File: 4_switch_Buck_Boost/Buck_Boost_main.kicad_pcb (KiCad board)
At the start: 2 copper layers, 12 parts, among them J1 Screw_Terminal_2x5.08, J2 Screw_Terminal_2x5.08, J3 Screw_Terminal_2x2.54, Q1 CSD18532Q5B, Q2 CSD18532Q5B, Q3 CSD18532Q5B, Q4 CSD18532Q5B, U1 LT8390EUFD_PBF

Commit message: Updated Schematic with cool stuff trust
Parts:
- removed F1, F2: Fuse_Holder_Auto, rsx_fuses:FUSE_3568-10
- removed HW1: Board_Mount_Heat_Sink_Screw_2.5C/W, rsx_misc:ATS-1139-C1-R0
- removed J1, J2: Screw_Terminal_2x5.08, rsx_headers_screw:Molex_0398800302
- removed J3: Screw_Terminal_2x2.54, rsx_headers_screw:Wurth_691210910002
- removed L1: 15u, rsx_inductors:PQ2617BHA-XXXK
- removed Q1, Q2, Q3, Q4: CSD18532Q5B, Package_TO_SOT_SMD:TDSON-8-1
- removed U1: LT8390EUFD_PBF, LT:QFN50P500X400X80-29N
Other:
- copper layers 2 -> 4
- board text removed: "Test1234"

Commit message: Updated the Component Placement
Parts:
- added C1: 4.7u, rsx_capacitors:C_0805_2012Metric, F.Cu at (71.5, 21.7)
- added C101: 4.7u, rsx_capacitors:C_0805_2012Metric, F.Cu at (71.5, 30.8)
- added C102: 0.1u, rsx_capacitors:C_0603_1608Metric, F.Cu at (32.7, 67.5)
- added C103: 0.47u, rsx_capacitors:C_0603_1608Metric, F.Cu at (32.7, 70.0)
- added C106: 4.7u, rsx_capacitors:C_0805_2012Metric, F.Cu at (71.5, 33.8)
- added C107: 47u, Capacitor_SMD:CP_Elec_8x10.5, F.Cu at (24.1, 25.2)
- added C108: 47u, Capacitor_SMD:CP_Elec_8x10.5, F.Cu at (24.1, 35.3)
- added C109: 33u, Capacitor_SMD:CP_Elec_8x10.5, F.Cu at (24.1, 45.4)
- added C110: 33u, Capacitor_SMD:CP_Elec_8x10.5, F.Cu at (24.1, 55.4)
- added C111: 33u, Capacitor_SMD:CP_Elec_8x10.5, F.Cu at (24.1, 65.5)
- added C112: 4.7u, rsx_capacitors:C_0805_2012Metric, F.Cu at (52.5, 140.4)
- added C113: 4.7u, rsx_capacitors:C_0805_2012Metric, F.Cu at (55.0, 140.4)
- added C114: 0.1u, rsx_capacitors:C_0603_1608Metric, F.Cu at (32.7, 72.5)
- added C115: 0.1u, rsx_capacitors:C_0603_1608Metric, F.Cu at (32.7, 75.0)
- added C116: 0.1u, rsx_capacitors:C_0603_1608Metric, F.Cu at (36.7, 57.4)
- added C117: 47u, Capacitor_SMD:CP_Elec_8x10.5, F.Cu at (24.1, 75.5)
- added C118: 0.1u, rsx_capacitors:C_0603_1608Metric, F.Cu at (57.0, 140.2)
- added C119: 100p, rsx_capacitors:C_0603_1608Metric, F.Cu at (36.7, 62.5)
- added C120: 4.7n, rsx_capacitors:C_0603_1608Metric, F.Cu at (36.7, 65.0)
- added C121: 0.1u, rsx_capacitors:C_0603_1608Metric, F.Cu at (36.7, 67.5)
- added C123: 470p, Capacitor_SMD:C_0805_2012Metric, F.Cu at (55.0, 133.0)
- added C124: 470p, Capacitor_SMD:C_0805_2012Metric, F.Cu at (97.5, 123.5)
- added C129: 0.1u, rsx_capacitors:C_0603_1608Metric, F.Cu at (36.7, 70.0)
- added C131: 22n, rsx_capacitors:C_0603_1608Metric, F.Cu at (36.7, 72.5)
- added C132: 0.1u, rsx_capacitors:C_0603_1608Metric, F.Cu at (59.0, 140.2)
- added C4: 22n, rsx_capacitors:C_0603_1608Metric, F.Cu at (61.0, 140.2)
- added C5: 0.1u, rsx_capacitors:C_0603_1608Metric, F.Cu at (32.7, 60.0)
- added C6: 1.0u, rsx_capacitors:C_0805_2012Metric, F.Cu at (71.5, 24.7)
- added C7: 1.0u, rsx_capacitors:C_0805_2012Metric, F.Cu at (71.5, 27.8)
- added C8: 0.47u, rsx_capacitors:C_0603_1608Metric, F.Cu at (32.7, 62.5)
- added C9: 0.47u, rsx_capacitors:C_0603_1608Metric, F.Cu at (32.7, 65.0)
- added D1: LED_G, rsx_leds:LED_0805_2012Metric, F.Cu at (24.3, 82.0)
- added D2: LED_G, rsx_leds:LED_0805_2012Metric, F.Cu at (24.3, 85.1)
- added D3: LED_G, rsx_leds:LED_0805_2012Metric, F.Cu at (24.3, 88.1)
- added F1: Fuse_Holder_Auto, Fuse:Fuseholder_Blade_Mini_Keystone_3568, F.Cu at (70.8, 58.6)
- added F2: Fuse_Holder_Auto, Fuse:Fuseholder_Blade_Mini_Keystone_3568, F.Cu at (70.8, 66.9)
- added F3: 40mm_by_20mm_Fan_Vertical, rsx_misc:40mmFan, F.Cu at (51.2, 51.7)
- added H1: M4 PLATED, MountingHole:MountingHole_3.2mm_M3_Pad_Via, F.Cu at (54.8, 60.2)
- added H2: M4 PLATED, MountingHole:MountingHole_3.2mm_M3_Pad_Via, F.Cu at (54.8, 68.1)
- added H3: M4 PLATED, MountingHole:MountingHole_3.2mm_M3_Pad_Via, F.Cu at (54.8, 76.1)
- added H4: M4 PLATED, MountingHole:MountingHole_3.2mm_M3_Pad_Via, F.Cu at (54.8, 84.0)
- added HW2: Board_Mount_Heat_Sink_Adhesive, rsx_misc:BDN10-3CB_A01, F.Cu at (31.5, 46.4)
- added J1: Conn_02x02_Counter_Clockwise, Connector_PinHeader_1.00mm:PinHeader_2x02_P1.00mm_Vertical, F.Cu at (66.2, 39.9)
- added J2: Screw_Terminal_2x5.08, rsx_headers_screw:Molex_0398800302, F.Cu at (60.9, 24.8)
- added J3: Screw_Terminal_2x2.54, rsx_headers_screw:Wurth_691210910002, F.Cu at (60.6, 42.3)
- added J4: Screw_Terminal_2x5.08, rsx_headers_screw:Molex_0398800302, F.Cu at (60.9, 33.8)
- added L1: 15u, Inductor_SMD:L_Wuerth_WE-XHMI-8080, F.Cu at (72.5, 128.5)
- added M1: Fan, Connector_Molex:Molex_KK-396_5273-02A_1x02_P3.96mm_Vertical, F.Cu at (69.6, 79.4)
- added NT1: NetTie_2, rsx_misc:NetTie-2_SMD_Pad0.5mm, F.Cu at (66.1, 43.4)
- added Q1: CSD18532Q5B, Package_TO_SOT_SMD:TDSON-8-1, F.Cu at (64.9, 138.1)
- added Q101: 2N7002K, rsx_packages_TO_SOT:SOT-23, F.Cu at (61.2, 85.2)
- added Q103: BSS83P, Package_TO_SOT_SMD:SOT-23, F.Cu at (80.6, 27.2)
- added Q2: CSD18532Q5B, Package_TO_SOT_SMD:TDSON-8-1, F.Cu at (103.8, 129.0)
- added Q3: CSD18532Q5B, Package_TO_SOT_SMD:TDSON-8-1, F.Cu at (59.0, 135.0)
- added Q4: CSD18532Q5B, Package_TO_SOT_SMD:TDSON-8-1, F.Cu at (94.8, 129.0)
- added Q6: AO3400A, Package_TO_SOT_SMD:SOT-23, F.Cu at (80.6, 22.6)
- added R1: 4.7k, rsx_resistors:R_0603_1608Metric, F.Cu at (40.8, 57.4)
- added R10: 50k, rsx_resistors:R_0603_1608Metric, F.Cu at (40.8, 75.0)
- added R103: 200k, rsx_resistors:R_0603_1608Metric, F.Cu at (44.8, 57.4)
- added R104: 10k, rsx_resistors:R_0603_1608Metric, F.Cu at (44.8, 60.0)
- added R105: 100K, rsx_resistors:R_0603_1608Metric, F.Cu at (44.8, 62.5)
- added R106: 100K, rsx_resistors:R_0603_1608Metric, F.Cu at (44.8, 65.0)
- added R107: 100K, rsx_resistors:R_0603_1608Metric, F.Cu at (44.8, 67.5)
- added R109: 100K, rsx_resistors:R_0603_1608Metric, F.Cu at (44.8, 70.0)
- added R110: 22k, rsx_resistors:R_0603_1608Metric, F.Cu at (44.8, 72.5)
- added R111: 56k, rsx_resistors:R_0603_1608Metric, F.Cu at (44.8, 75.0)
- added R112: 100k, rsx_resistors:R_0603_1608Metric, F.Cu at (48.8, 57.4)
- added R113: 4.7, Capacitor_SMD:C_0805_2012Metric, F.Cu at (55.0, 136.5)
- added R114: 4.7, Capacitor_SMD:C_0805_2012Metric, F.Cu at (93.0, 123.5)
- added R115: 4.7, rsx_resistors:R_0603_1608Metric, F.Cu at (62.0, 124.0)
- added R116: 4.7, rsx_resistors:R_0603_1608Metric, F.Cu at (47.0, 138.0)
- added R117: 4.7, rsx_resistors:R_0603_1608Metric, F.Cu at (61.5, 147.5)
- added R118: 4.7, rsx_resistors:R_0603_1608Metric, F.Cu at (48.8, 67.5)
- added R2: 4.7k, rsx_resistors:R_0603_1608Metric, F.Cu at (40.8, 60.0)
- added R3: 4.7k, rsx_resistors:R_0603_1608Metric, F.Cu at (40.8, 62.5)
- added R4: 100K, rsx_resistors:R_0603_1608Metric, F.Cu at (40.8, 65.0)
- added R5: 10k, rsx_resistors:R_0603_1608Metric, F.Cu at (40.8, 67.5)
- added R6: 100, rsx_resistors:R_0603_1608Metric, F.Cu at (40.8, 70.0)
- added R9: 300k, rsx_resistors:R_0603_1608Metric, F.Cu at (40.8, 72.5)
- added RV101: 50k, Potentiometer_SMD:Potentiometer_Bourns_3314G_Vertical, F.Cu at (72.3, 42.5)
- added RV102: 50k, Potentiometer_SMD:Potentiometer_Bourns_3314G_Vertical, F.Cu at (78.3, 42.5)
- added TH1: 10k, Connector_Molex:Molex_KK-396_5273-02A_1x02_P3.96mm_Vertical, F.Cu at (78.8, 79.4)
- added TP1: BAT, TestPoint:TestPoint_2Pads_Pitch2.54mm_Drill0.8mm, F.Cu at (80.0, 31.1)
- added TP10: EN, TestPoint:TestPoint_Pad_D1.0mm, F.Cu at (48.2, 77.8)
- added TP11: Output, TestPoint:TestPoint_2Pads_Pitch2.54mm_Drill0.8mm, F.Cu at (80.0, 34.5)
- added TP12: GND, TestPoint:TestPoint_Pad_D1.0mm, F.Cu at (48.2, 80.8)
- added TP13: GNDA, TestPoint:TestPoint_Pad_D1.0mm, F.Cu at (48.2, 83.9)
- added TP2: GND, TestPoint:TestPoint_Pad_D1.0mm, F.Cu at (42.1, 77.8)
- added TP3: SW1, TestPoint:TestPoint_Loop_D1.80mm_Drill1.0mm_Beaded, F.Cu at (19.7, 82.8)
- added TP4: SW2, TestPoint:TestPoint_Loop_D1.80mm_Drill1.0mm_Beaded, F.Cu at (101.0, 117.0)
- added TP5: RT, TestPoint:TestPoint_Pad_D1.0mm, F.Cu at (42.1, 80.8)
- added TP6: FB, TestPoint:TestPoint_Pad_D1.0mm, F.Cu at (42.1, 83.9)
- added TP7: Vout, TestPoint:TestPoint_Pad_D1.0mm, F.Cu at (45.1, 77.8)
- added TP8: Vin, TestPoint:TestPoint_Pad_D1.0mm, F.Cu at (45.1, 80.8)
- added TP9: GND, TestPoint:TestPoint_Pad_D1.0mm, F.Cu at (45.1, 83.9)
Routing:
- net Vin: track 0.00 -> 8.64 mm
- net GND: track 0.00 -> 8.50 mm, vias 0 -> 15
- net Net-(C124-Pad2): track 0.00 -> 2.65 mm
- net Net-(C123-Pad2): track 0.00 -> 2.07 mm
- added copper zone on F.Cu, net GND
- added copper zone on In1.Cu, net GND
- added copper zone on In2.Cu, net SW2

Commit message: pcb - lets pray
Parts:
- added R7: 6m, shunt:RES_KRL3216T4-M-R003-F-T1, F.Cu at (75.7, 138.2)
- added R8: 15m, shunt:RES_KRL3216T4-M-R003-F-T1, F.Cu at (67.5, 109.0)
- added U1: LT8390EUFD_PBF, LT:QFN50P500X400X80-29N, F.Cu at (77.7, 131.1)
- moved C129 88.1 mm to (90.8, 139.6), turned to 180 degrees
- moved C131 84.8 mm to (90.8, 137.8), turned to 180 degrees
- moved R118 71.7 mm to (84.4, 129.8)
- moved R116 27.3 mm to (73.2, 130.3), turned to -90 degrees
- moved Q2 21.4 mm to (88.1, 143.5)
- moved R117 20.2 mm to (79.0, 137.4)
- moved L1 17.8 mm to (79.4, 144.9)
- moved C124 17.3 mm to (83.3, 133.4), turned to 0 degrees
- moved C123 16.9 mm to (71.9, 133.2), turned to 180 degrees
- moved C112 16.6 mm to (66.1, 149.9), turned to 180 degrees
- moved R113 13.7 mm to (68.3, 133.1), turned to 180 degrees
- moved C113 13.1 mm to (66.1, 147.4), turned to 180 degrees
- moved Q4 12.9 mm to (85.2, 137.5), turned to 180 degrees
- moved R114 11.6 mm to (86.9, 133.3), turned to 0 degrees
- moved Q3 11.5 mm to (70.3, 137.1), turned to 0 degrees
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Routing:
- net Net-(C124-Pad2): track 2.65 -> 0.00 mm
- net Net-(C123-Pad2): track 2.07 -> 0.00 mm
- net GND: vias 15 -> 0
- removed copper zone on F.Cu, net GND
- removed copper zone on In2.Cu, net SW2

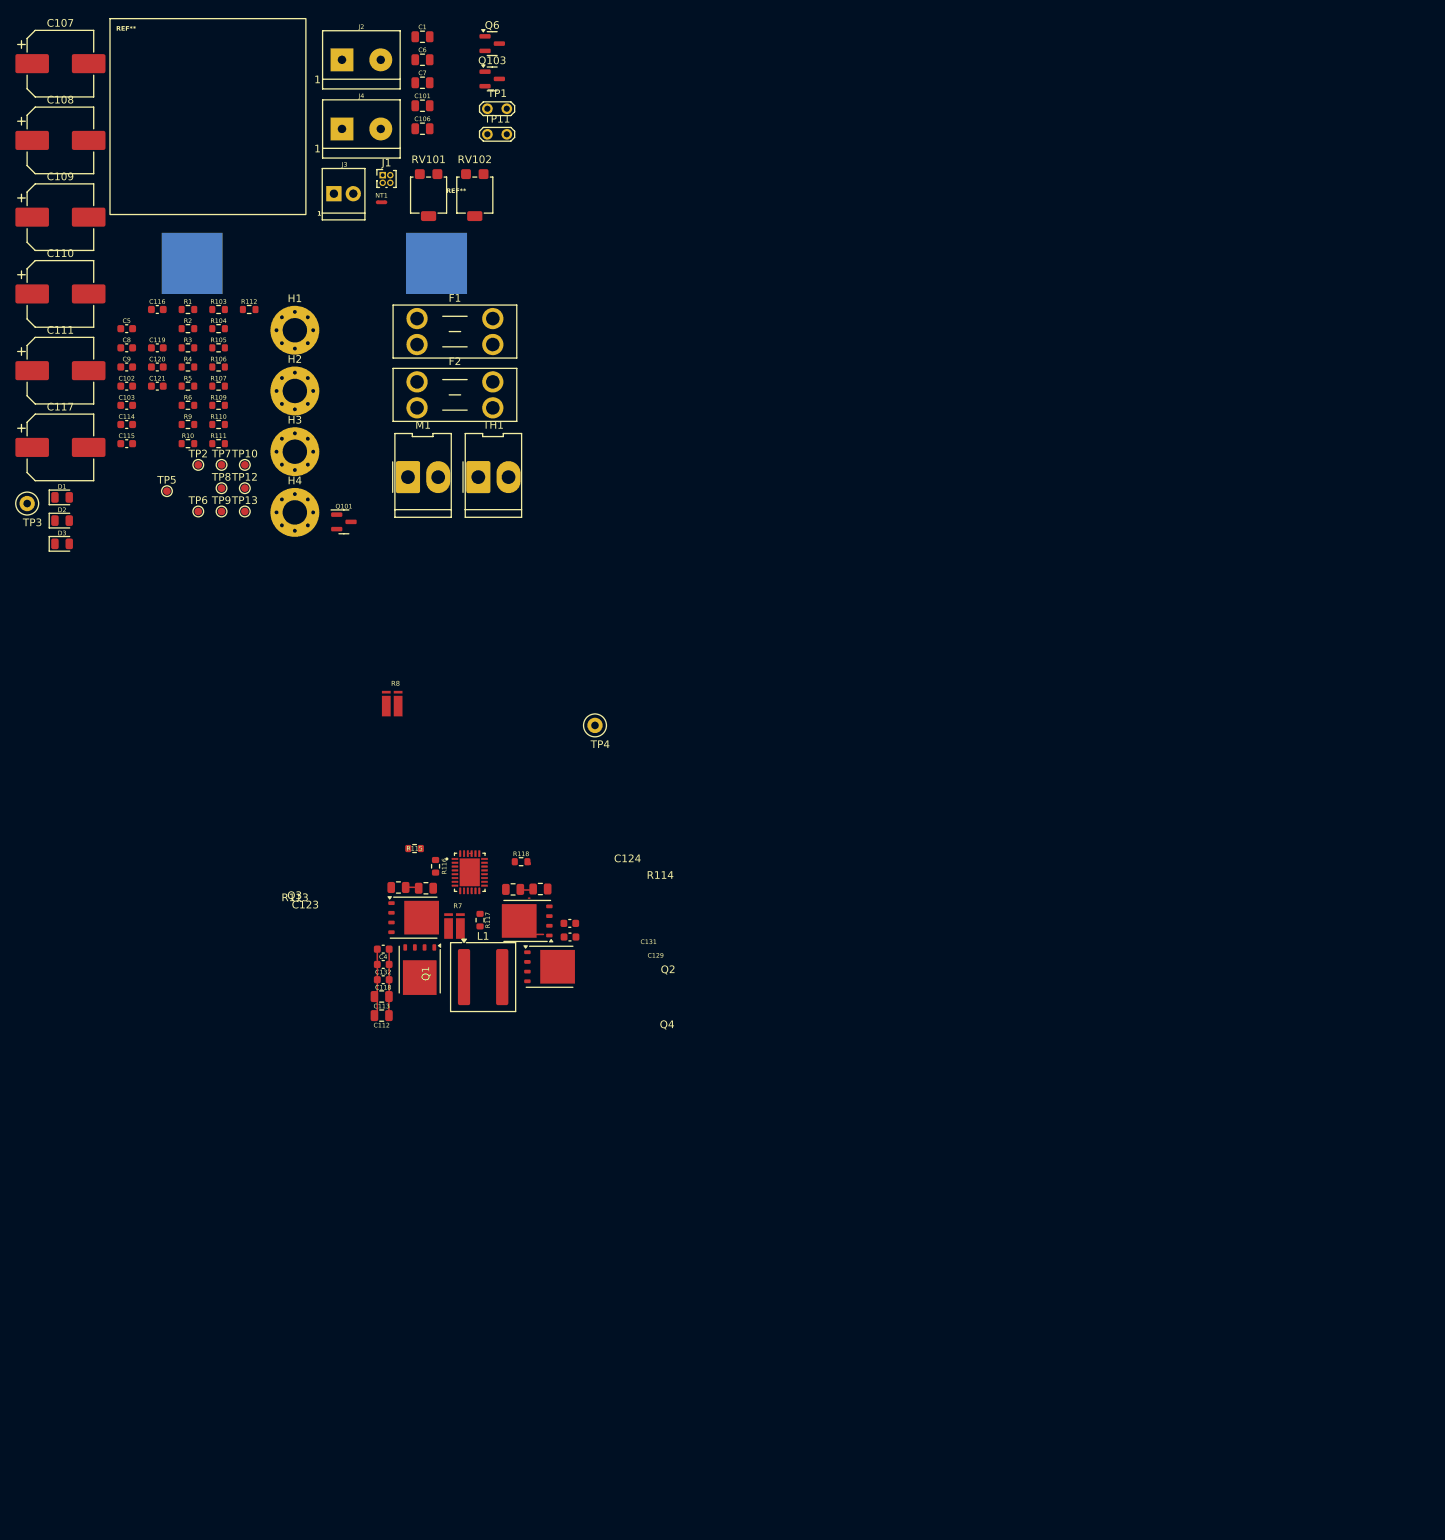
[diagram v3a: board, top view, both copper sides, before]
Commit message: Edited component placement. Added general sketch for the power path. Removed some traces.
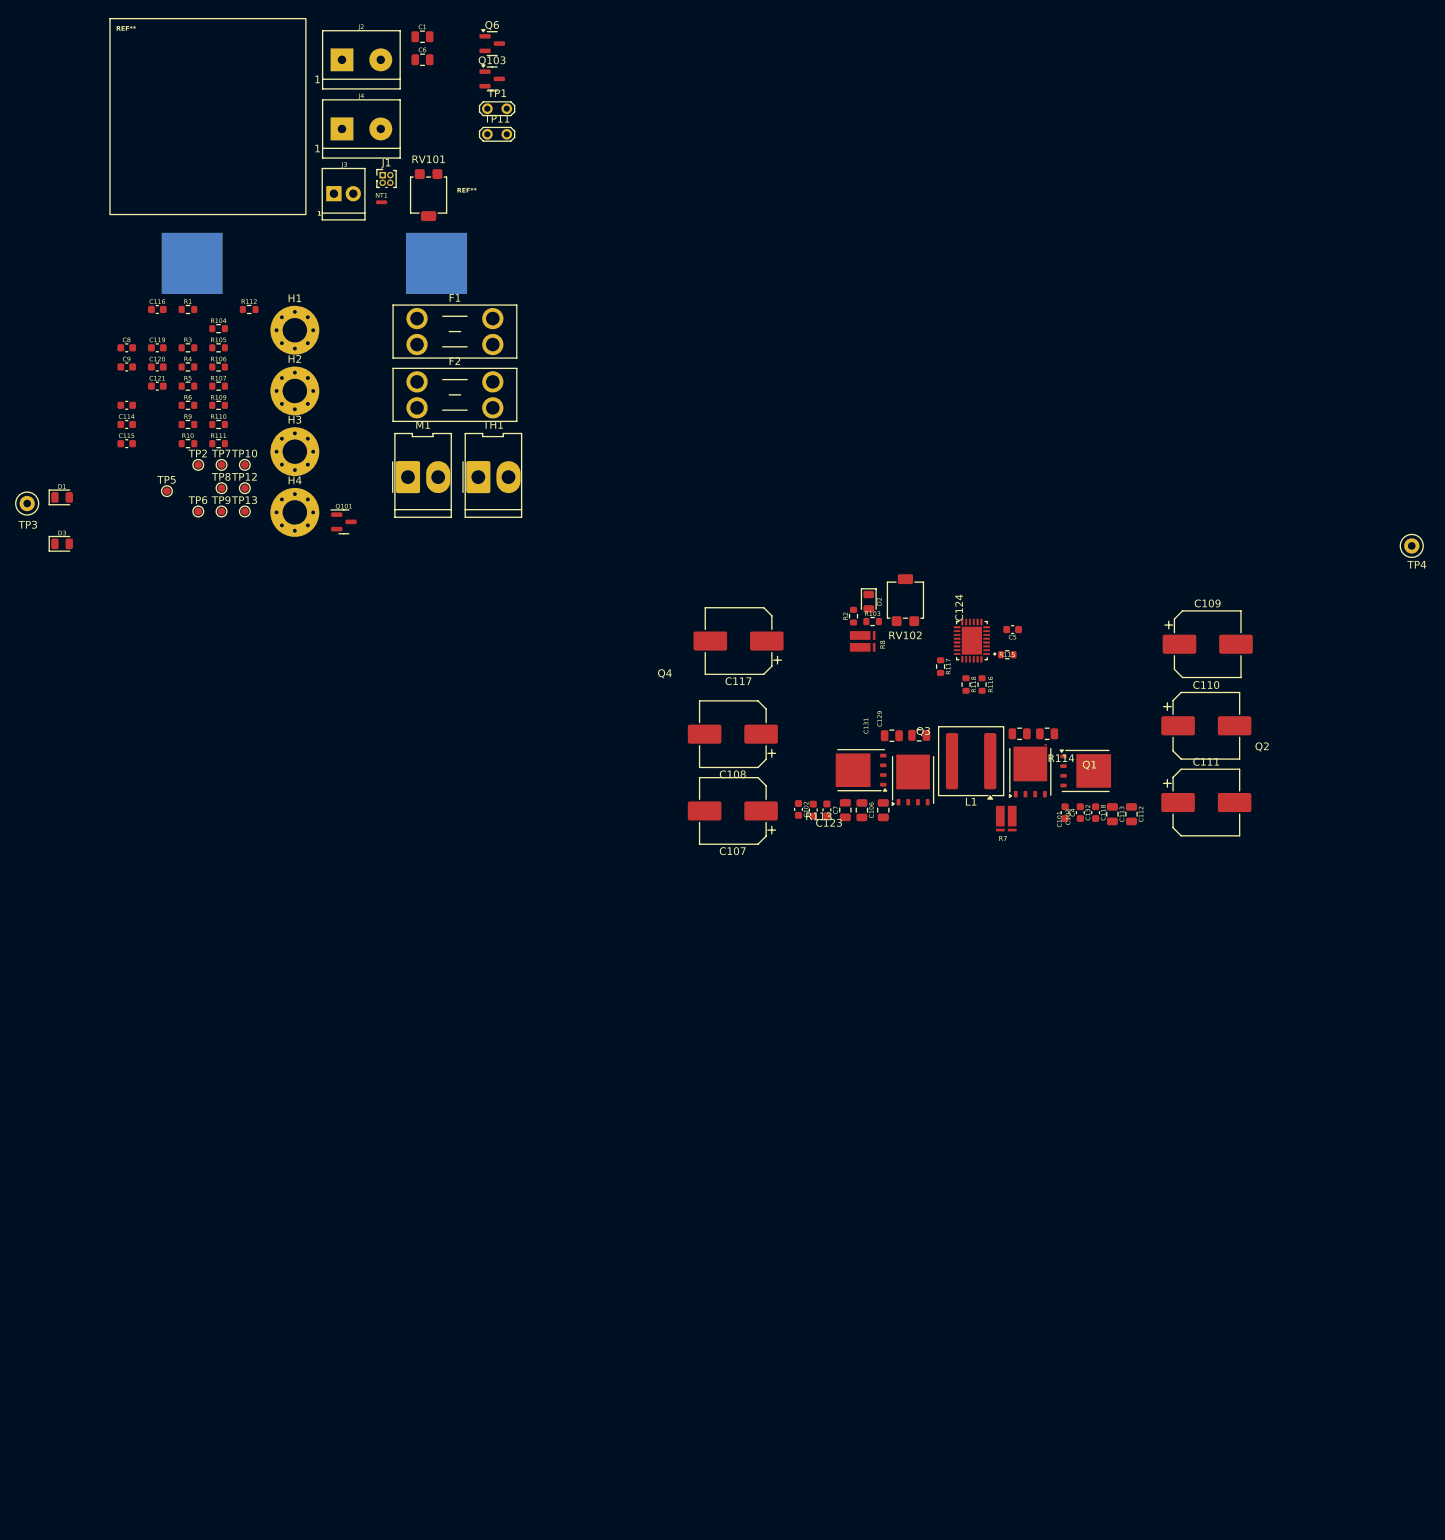
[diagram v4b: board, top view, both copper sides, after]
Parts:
- moved C110 160.4 mm to (174.1, 112.0)
- moved C111 160.4 mm to (174.1, 122.0)
- moved C109 160.3 mm to (174.3, 101.3)
- moved C107 131.6 mm to (112.1, 123.1), turned to 180 degrees
- moved C5 122.5 mm to (148.7, 99.3), turned to 180 degrees
- moved C108 117.5 mm to (112.1, 113.0), turned to 180 degrees
- moved C101 110.2 mm to (131.8, 123.0), turned to -90 degrees
- moved C7 110.2 mm to (126.8, 123.0), turned to 90 degrees
- moved TP4 109.5 mm to (201.0, 88.4)
- moved C106 106.2 mm to (129.0, 123.0), turned to -90 degrees
- moved D2 106.2 mm to (129.9, 95.7), turned to -90 degrees
- moved C102 104.0 mm to (120.7, 122.9), turned to -90 degrees
- moved C112 101.7 mm to (164.3, 123.5), turned to -90 degrees
- moved C113 98.6 mm to (161.8, 123.5), turned to -90 degrees
- moved C118 95.8 mm to (159.6, 123.3), turned to -90 degrees
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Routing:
- net GND: track 8.50 -> 0.00 mm
- net Vin: track 8.64 -> 0.49 mm

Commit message: controller and auxiliary circuits
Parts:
- moved D1 152.2 mm to (176.0, 93.8), turned to 180 degrees
- moved R1 136.2 mm to (172.1, 93.7)
- moved D3 134.6 mm to (158.8, 92.1)
- moved C116 132.4 mm to (166.0, 86.0)
- moved C114 128.5 mm to (161.2, 71.6), turned to 180 degrees
- moved TP4 126.6 mm to (74.4, 90.5)
- moved C115 126.0 mm to (158.3, 84.8), turned to 180 degrees
- moved R3 124.1 mm to (161.4, 91.1), turned to -90 degrees
- moved C8 123.4 mm to (147.6, 107.5)
- moved J2 122.8 mm to (176.6, 66.0), turned to 180 degrees
- moved R106 121.7 mm to (165.1, 83.4), turned to 90 degrees
- moved R9 121.6 mm to (161.4, 87.5), turned to -90 degrees
- moved C103 121.5 mm to (152.1, 92.7), turned to -90 degrees
- moved R10 117.9 mm to (157.9, 88.5), turned to 180 degrees
- moved R105 116.9 mm to (160.3, 80.4)
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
